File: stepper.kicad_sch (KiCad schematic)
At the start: 10 parts, among them M2 Stepper_Motor_bipolar, U6 DRV8424RGER

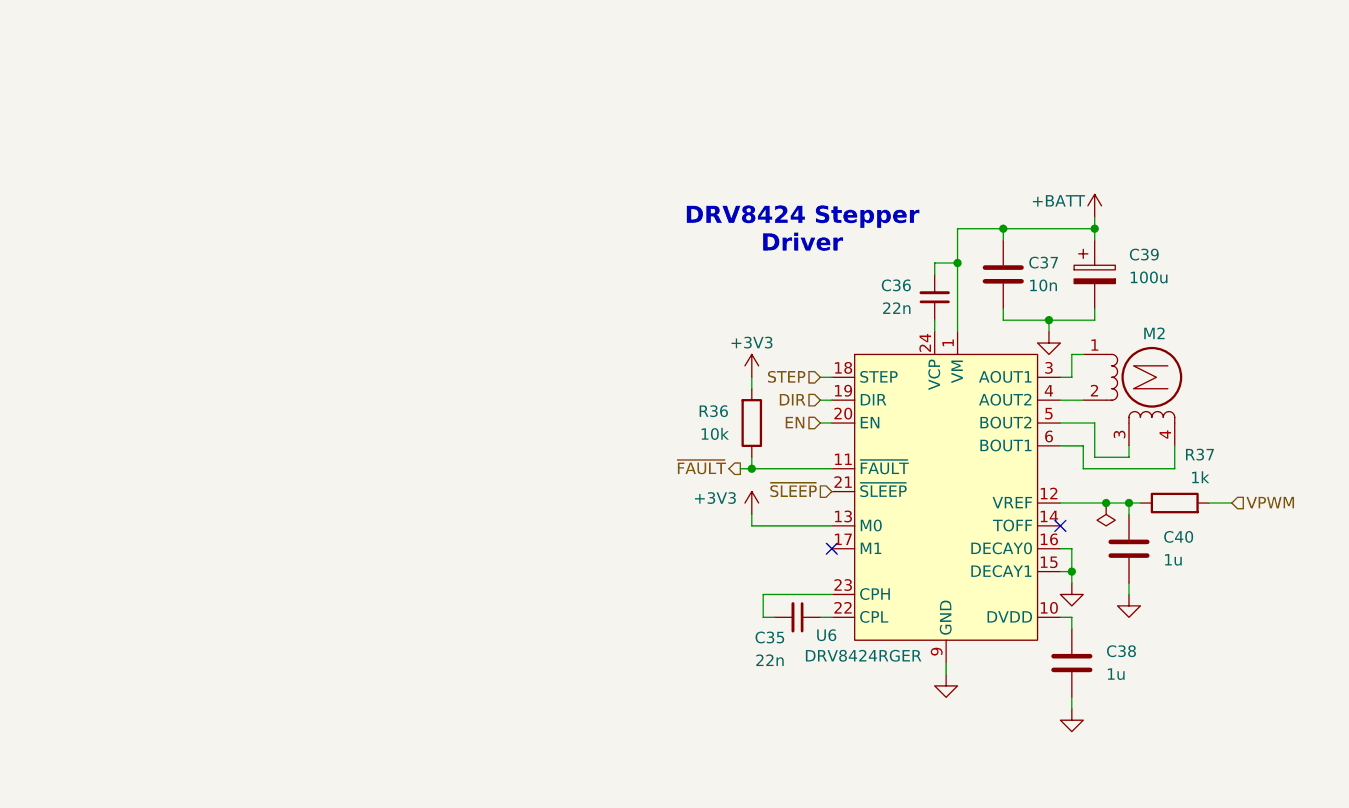
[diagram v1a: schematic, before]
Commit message: schem: add TMC2209 Stepper driver
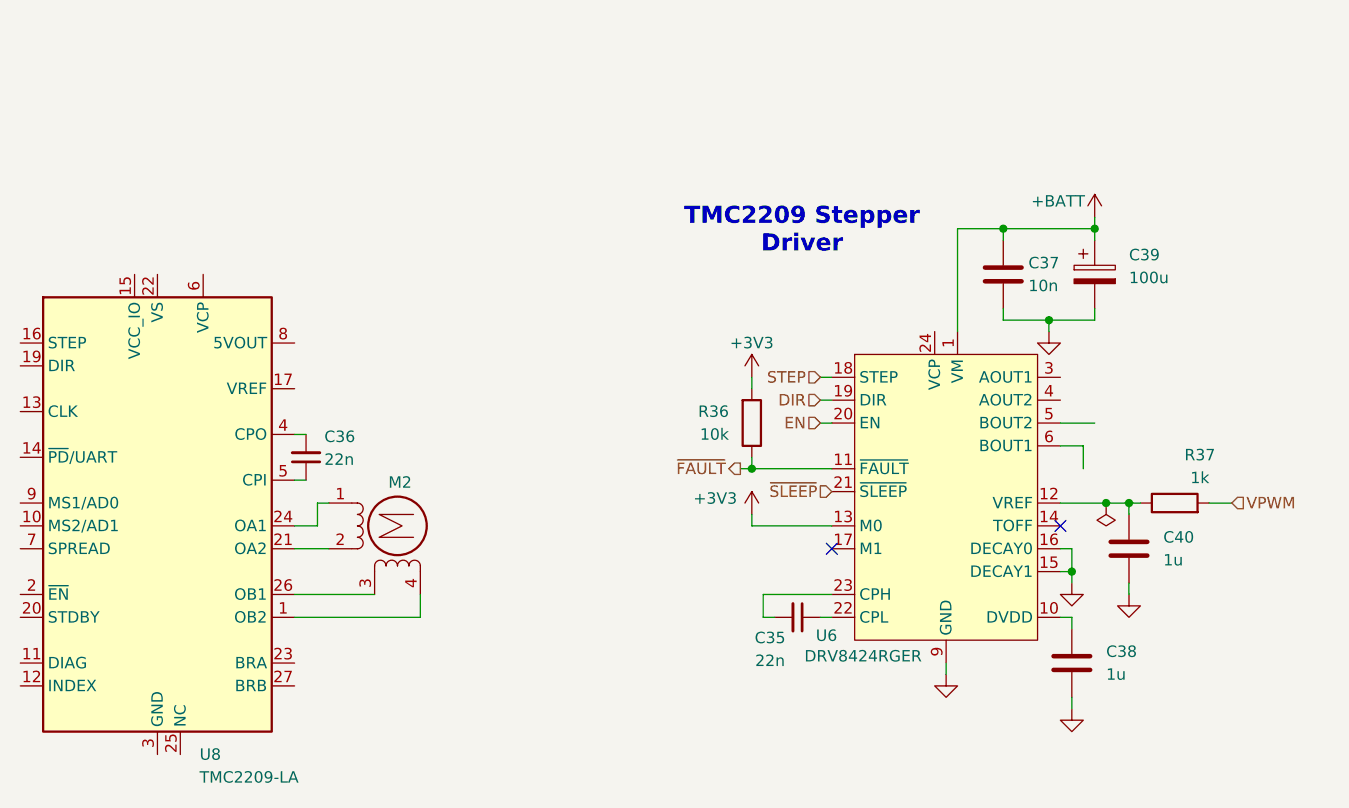
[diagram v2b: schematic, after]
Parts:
- added U8: TMC2209-LA, Package_DFN_QFN:VQFN-28-1EP_5x5mm_P0.5mm_EP3.7x3.7mm_ThermalVias, symbol Driver_Motor:TMC2209-LA
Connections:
- net +BATT: no longer C36.2
- net at M2.1 (-): now also U8.24 (OA1); no longer U6.3 (AOUT1)
- net at M2.2: now also U8.21 (OA2); no longer U6.4 (AOUT2)
- net at M2.3: now also U8.26 (OB1); no longer U6.5 (BOUT2)
- net at M2.4: now also U8.1 (OB2); no longer U6.6 (BOUT1)
- net at C36.1: now also U8.5 (CPI); no longer U6.24 (VCP)
- new net: C36.2, U8.4 (CPO)
- new net: U8.18 (GND), U8.29 (GND), U8.3 (GND)
- new net: U8.22 (VS), U8.28 (VS)
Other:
- note added: "TMC2209 Stepper Driver"
- note removed: "DRV8424 Stepper Driver"
- moved on the sheet: C36, M2

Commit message: schem: connect new stepper driver to mcu
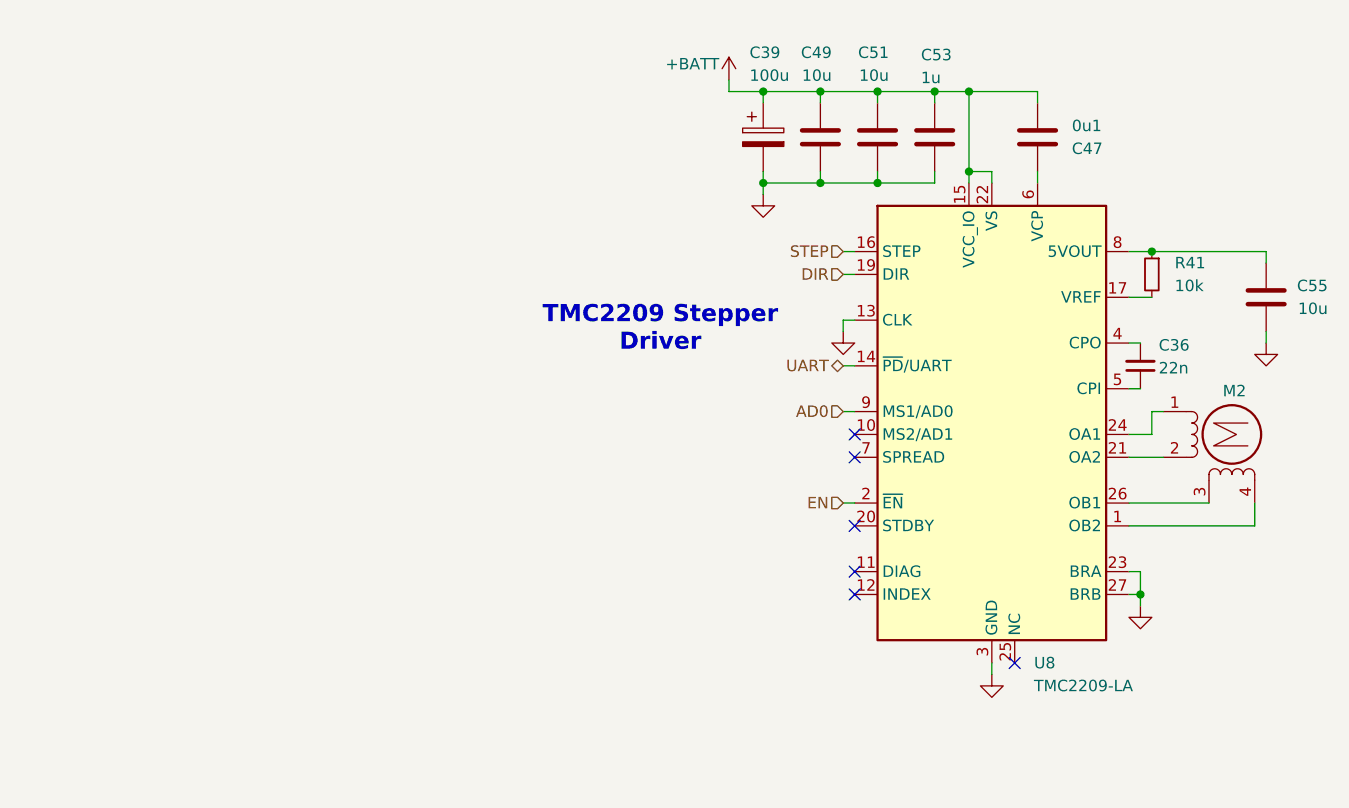
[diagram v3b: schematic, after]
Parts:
- removed C35: 22n, Capacitor_SMD:C_0402_1005Metric, symbol Device:C_Small
- removed C37: 10n, Capacitor_SMD:C_0402_1005Metric, symbol Device:C
- removed C38, C40: 1u, Capacitor_SMD:C_0402_1005Metric, symbol Device:C
- removed R36: 10k, Resistor_SMD:R_0402_1005Metric, symbol Device:R
- removed R37: 1k, Resistor_SMD:R_0402_1005Metric, symbol Device:R
- removed U6: DRV8424RGER, GLCS:Texas_RGE0024B_VQFN-24-1EP_4x4mm_P0.5mm_EP2.5x2.5mm_ThermalVias, symbol GLCS:DRV8424RGER
- added C47: 0u1, Capacitor_SMD:C_0402_1005Metric, symbol Device:C
- added C49, C51, C55: 10u, Capacitor_SMD:C_0805_2012Metric, symbol Device:C
- added C53: 1u, Capacitor_SMD:C_0402_1005Metric, symbol Device:C
- added R41: 10k, Resistor_SMD:R_0402_1005Metric, symbol Device:R_Small
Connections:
- net +BATT: now also U8.15 (VCC_IO), U8.22 (VS), U8.28 (VS), C47.1, C49.1, C51.1, C53.1
- net DIR: now also U8.19 (DIR)
- net EN: now also U8.2 (~{EN})
- net GND: now also U8.13 (CLK), U8.18 (GND), U8.23 (BRA), U8.27 (BRB), U8.29 (GND), U8.3 (GND), C49.2, C51.2, C53.2, C55.2
- net STEP: now also U8.16 (STEP)
- net UART: now reaches U8.14 (~{PD}/UART)
- net at U8.17 (VREF): now also R41.2
- net at U8.6 (VCP): now also C47.2
- net at U8.8 (5VOUT): now also C55.1, R41.1
- net AD0: now reaches U8.9 (MS1/AD0)
- no-connect marks 2 -> 6
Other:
- moved on the sheet: C36, C39, M2, U8

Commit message: schem: add ordering info to BOM
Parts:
- U8: Basic (none) -> X; JLCPCB Part # (none) -> C2150710; Manufacturer (none) -> Trinamic; Manufacturer Part Number (none) -> TMC2209-LA-T
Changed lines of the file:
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@@
+			)
+		)
+		(property "Basic" "X"
+			(at 152.4 97.79 0)
+			(hide yes)
+			(show_name no)
+			(do_not_autoplace no)
+			(effects
+				(font
+					(size 1.27 1.27)
+				)
+			)
+		)
+		(property "JLCPCB Part #" "C2150710"
+			(at 152.4 97.79 0)
+			(hide yes)
+			(show_name no)
+			(do_not_autoplace no)
+			(effects
+				(font
+					(size 1.27 1.27)
+				)
+			)
+		)
+		(property "Manufacturer" "Trinamic"
+			(at 152.4 97.79 0)
+			(hide yes)
+			(show_name no)
+			(do_not_autoplace no)
+			(effects
+				(font
+					(size 1.27 1.27)
+				)
+			)
+		)
+		(property "Manufacturer Part Number" "TMC2209-LA-T"
+			(at 152.4 97.79 0)
+			(hide yes)
+			(show_name no)
+			(do_not_autoplace no)
+			(effects
+				(font
+					(size 1.27 1.27)
+				)
 			)
 		)

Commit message: pcb: add new drivers layout
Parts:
- removed C51, C55: 10u, Capacitor_SMD:C_0805_2012Metric, symbol Device:C
- added C35: 4u7, Capacitor_SMD:C_0402_1005Metric, symbol Device:C
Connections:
- net GND: now also C35.2
- net at M2.1 (-): now also U8.21 (OA2); no longer U8.24 (OA1)
- net at M2.2: now also U8.24 (OA1); no longer U8.21 (OA2)
- net at R41.1, U8.8 (5VOUT): now also C35.1
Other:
- moved on the sheet: C39, C49

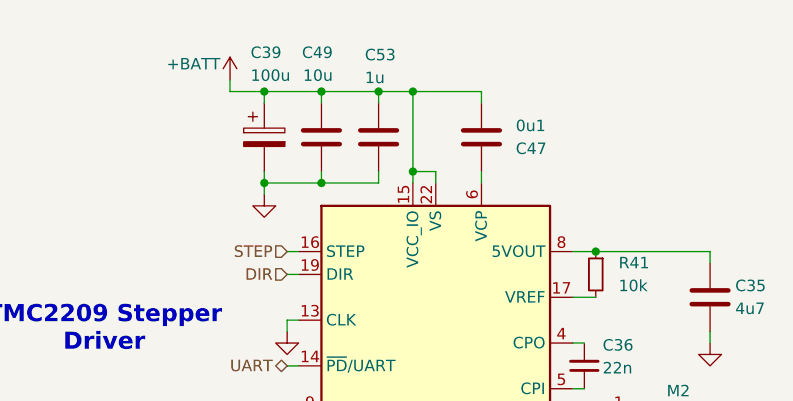
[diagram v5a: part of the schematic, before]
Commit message: schem/pcb: fix stepper driver vcc_io voltage
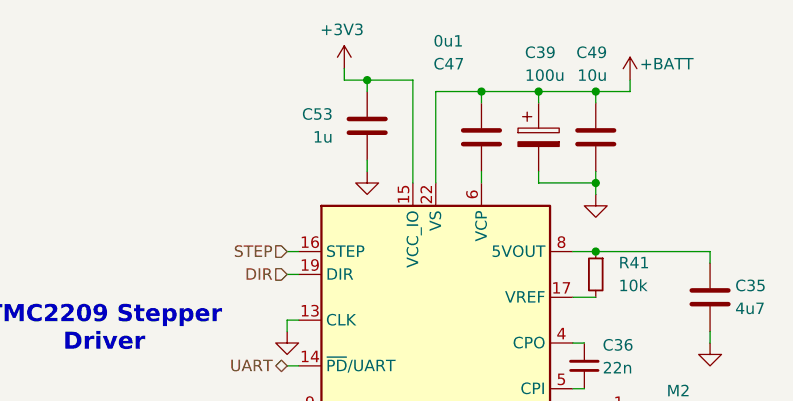
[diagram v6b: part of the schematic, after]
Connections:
- net +BATT: no longer C53.1, U8.15 (VCC_IO)
- new net +3V3: C53.1, U8.15 (VCC_IO)
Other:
- moved on the sheet: C39, C49, C53

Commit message: rev02
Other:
- company: (none) -> Valrobotik
- title: (none) -> Carte Pami CDF 1
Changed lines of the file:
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@@
 	(generator_version "10.0")
 	(paper "A4")
+	(title_block
+		(title "Carte Pami CDF 1")
+		(date "2026-04-11")
+		(rev "02")
+		(company "Valrobotik")
+	)
 	(text "TMC2209 Stepper\nDriver"
 		(exclude_from_sim no)
